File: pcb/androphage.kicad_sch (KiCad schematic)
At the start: 86 parts, among them J1 VIK_OUT, J11 VIK_OUT_SENSOR, J12 Conn_01x04, J13 Conn_01x02, J2 Conn_01x04, J3 USB_C_Receptacle_USB2.0_16P, Q1 AO3401A, Q2 AO3401A, SW00 SW_Push_45deg, SW01 SW_Push_45deg, SW02 SW_Push_45deg, SW03 SW_Push_45deg, SW04 SW_Push_45deg, SW05 SW_Push_45deg, SW10 SW_Push_45deg, SW11 SW_Push_45deg, SW12 SW_Push_45deg, SW13 SW_Push_45deg, SW14 SW_Push_45deg, SW15 SW_Push_45deg, SW20 SW_Push_45deg, SW21 SW_Push_45deg, SW22 SW_Push_45deg, SW23 SW_Push_45deg, SW24 SW_Push_45deg, SW25 SW_Push_45deg, SW30 SW_Push_45deg, SW31 SW_Push_45deg, SW32 SW_Push_45deg, SW33 SW_Push_45deg, SW34 SW_Push_45deg, SW35 SW_Push_45deg, SW6 SW_Push, SW7 SW_SPST, U1 holyiot-18010-no-underside, U2 MCP73832-2-OT, U3 XC6220B331MR, U4 SRV05-4, U6 MCP23017_SS

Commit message: Update key switch footprint.
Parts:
- SW00, SW01, SW02, SW03, SW04, SW10, SW11, SW12, SW13, SW14, SW15, SW20, SW21, SW22, SW23, SW24, SW25, SW31, SW32, SW33, SW34, SW35: footprint key-switches:SW_GLP_Kailh_Choc_V1V2_HotSwap_double -> key-switches:SW_Kailh_Choc_V1V2_HotSwap_PTH_Double
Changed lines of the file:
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@@
 			)
 		)
-		(property "Footprint" "key-switches:SW_GLP_Kailh_Choc_V1V2_HotSwap_double"
+		(property "Footprint" "key-switches:SW_Kailh_Choc_V1V2_HotSwap_PTH_Double"
 			(at 215.9 266.7 0)
 			(effects
@@
 		)
 		(instances
-			(project ""
+			(project "androphage"
 				(path "/99196bd8-ec0c-4029-b5c4-fcab8025953e"
 					(reference "R2")
@@
 		)
 		(instances
-			(project ""
+			(project "androphage"
 				(path "/99196bd8-ec0c-4029-b5c4-fcab8025953e"
 					(reference "R8")
@@
 			)
 		)
-		(property "Footprint" "key-switches:SW_GLP_Kailh_Choc_V1V2_HotSwap_double"
+		(property "Footprint" "key-switches:SW_Kailh_Choc_V1V2_HotSwap_PTH_Double"
 			(at 127 251.46 0)
 			(effects
@@
 		)
 		(instances
-			(project ""
+			(project "androphage"
 				(path "/99196bd8-ec0c-4029-b5c4-fcab8025953e"
 					(reference "U4")
@@
 		)
 		(instances
-			(project ""
+			(project "androphage"
 				(path "/99196bd8-ec0c-4029-b5c4-fcab8025953e"
 					(reference "R9")
@@
 			)
 		)
-		(property "Footprint" "key-switches:SW_GLP_Kailh_Choc_V1V2_HotSwap_double"
+		(property "Footprint" "key-switches:SW_Kailh_Choc_V1V2_HotSwap_PTH_Double"
 			(at 198.12 234.95 0)
 			(effects
@@
 		)
 		(instances
-			(project ""
+			(project "androphage"
 				(path "/99196bd8-ec0c-4029-b5c4-fcab8025953e"
 					(reference "R10")
@@
 			)
 		)
-		(property "Footprint" "key-switches:SW_GLP_Kailh_Choc_V1V2_HotSwap_double"
+		(property "Footprint" "key-switches:SW_Kailh_Choc_V1V2_HotSwap_PTH_Double"
 			(at 215.9 251.46 0)
 			(effects
@@
 			)
 		)
-		(property "Footprint" "key-switches:SW_GLP_Kailh_Choc_V1V2_HotSwap_double"
+		(property "Footprint" "key-switches:SW_Kailh_Choc_V1V2_HotSwap_PTH_Double"
 			(at 215.9 234.95 0)
 			(effects
@@
 		)
 		(instances
-			(project ""
+			(project "androphage"
 				(path "/99196bd8-ec0c-4029-b5c4-fcab8025953e"
 					(reference "D2")
@@
 			)
 		)
-		(property "Footprint" "key-switches:SW_GLP_Kailh_Choc_V1V2_HotSwap_double"
+		(property "Footprint" "key-switches:SW_Kailh_Choc_V1V2_HotSwap_PTH_Double"
 			(at 127 234.95 0)
 			(effects
@@
 		)
 		(instances
-			(project ""
+			(project "androphage"
 				(path "/99196bd8-ec0c-4029-b5c4-fcab8025953e"
 					(reference "SW6")
@@
 			)
 		)
-		(property "Footprint" "key-switches:SW_GLP_Kailh_Choc_V1V2_HotSwap_double"
+		(property "Footprint" "key-switches:SW_Kailh_Choc_V1V2_HotSwap_PTH_Double"
 			(at 144.78 266.7 0)
 			(effects
@@
 		)
 		(instances
-			(project ""
+			(project "androphage"
 				(path "/99196bd8-ec0c-4029-b5c4-fcab8025953e"
 					(reference "R11")
@@
 		)
 		(instances
-			(project ""
+			(project "androphage"
 				(path "/99196bd8-ec0c-4029-b5c4-fcab8025953e"
 					(reference "R12")
@@
 		)
 		(instances
-			(project ""
+			(project "androphage"
 				(path "/99196bd8-ec0c-4029-b5c4-fcab8025953e"
 					(reference "U2")
@@
 		)
 		(instances
-			(project ""
+			(project "androphage"
 				(path "/99196bd8-ec0c-4029-b5c4-fcab8025953e"
 					(reference "J2")
@@
 			)
 		)
-		(property "Footprint" "key-switches:SW_GLP_Kailh_Choc_V1V2_HotSwap_double"
+		(property "Footprint" "key-switches:SW_Kailh_Choc_V1V2_HotSwap_PTH_Double"
 			(at 162.56 234.95 0)
 			(effects
@@
 			)
 		)
-		(property "Footprint" "key-switches:SW_GLP_Kailh_Choc_V1V2_HotSwap_double"
+		(property "Footprint" "key-switches:SW_Kailh_Choc_V1V2_HotSwap_PTH_Double"
 			(at 127 219.71 0)
 			(effects
@@
 			)
 		)
-		(property "Footprint" "key-switches:SW_GLP_Kailh_Choc_V1V2_HotSwap_double"
+		(property "Footprint" "key-switches:SW_Kailh_Choc_V1V2_HotSwap_PTH_Double"
 			(at 180.34 266.7 0)
 			(effects
@@
 			)
 		)
-		(property "Footprint" "key-switches:SW_GLP_Kailh_Choc_V1V2_HotSwap_double"
+		(property "Footprint" "key-switches:SW_Kailh_Choc_V1V2_HotSwap_PTH_Double"
 			(at 144.78 251.46 0)
 			(effects
@@
 		)
 		(instances
-			(project ""
+			(project "androphage"
 				(path "/99196bd8-ec0c-4029-b5c4-fcab8025953e"
 					(reference "JP1")
@@
 			)
 		)
-		(property "Footprint" "key-switches:SW_GLP_Kailh_Choc_V1V2_HotSwap_double"
+		(property "Footprint" "key-switches:SW_Kailh_Choc_V1V2_HotSwap_PTH_Double"
 			(at 198.12 219.71 0)
 			(effects
@@
 			)
 		)
-		(property "Footprint" "key-switches:SW_GLP_Kailh_Choc_V1V2_HotSwap_double"
+		(property "Footprint" "key-switches:SW_Kailh_Choc_V1V2_HotSwap_PTH_Double"
 			(at 144.78 234.95 0)
 			(effects
@@
 			)
 		)
-		(property "Footprint" "key-switches:SW_GLP_Kailh_Choc_V1V2_HotSwap_double"
+		(property "Footprint" "key-switches:SW_Kailh_Choc_V1V2_HotSwap_PTH_Double"
 			(at 180.34 234.95 0)
 			(effects
@@
 		)
 		(instances
-			(project ""
+			(project "androphage"
 				(path "/99196bd8-ec0c-4029-b5c4-fcab8025953e"
 					(reference "J3")
@@
 			)
 		)
-		(property "Footprint" "key-switches:SW_GLP_Kailh_Choc_V1V2_HotSwap_double"
+		(property "Footprint" "key-switches:SW_Kailh_Choc_V1V2_HotSwap_PTH_Double"
 			(at 180.34 251.46 0)
 			(effects
@@
 			)
 		)
-		(property "Footprint" "key-switches:SW_GLP_Kailh_Choc_V1V2_HotSwap_double"
+		(property "Footprint" "key-switches:SW_Kailh_Choc_V1V2_HotSwap_PTH_Double"
 			(at 162.56 266.7 0)
 			(effects
@@
 			)
 		)
-		(property "Footprint" "key-switches:SW_GLP_Kailh_Choc_V1V2_HotSwap_double"
+		(property "Footprint" "key-switches:SW_Kailh_Choc_V1V2_HotSwap_PTH_Double"
 			(at 198.12 266.7 0)
 			(effects
@@
 		)
 		(instances
-			(project ""
+			(project "androphage"
 				(path "/99196bd8-ec0c-4029-b5c4-fcab8025953e"
 					(reference "Q1")
@@
 			)
 		)
-		(property "Footprint" "key-switches:SW_GLP_Kailh_Choc_V1V2_HotSwap_double"
+		(property "Footprint" "key-switches:SW_Kailh_Choc_V1V2_HotSwap_PTH_Double"
 			(at 162.56 251.46 0)
 			(effects
@@
 			)
 		)
-		(property "Footprint" "key-switches:SW_GLP_Kailh_Choc_V1V2_HotSwap_double"
+		(property "Footprint" "key-switches:SW_Kailh_Choc_V1V2_HotSwap_PTH_Double"
 			(at 144.78 219.71 0)
 			(effects
@@
 		)
 		(instances
-			(project ""
+			(project "androphage"
 				(path "/99196bd8-ec0c-4029-b5c4-fcab8025953e"
 					(reference "U3")
@@
 			)
 		)
-		(property "Footprint" "key-switches:SW_GLP_Kailh_Choc_V1V2_HotSwap_double"
+		(property "Footprint" "key-switches:SW_Kailh_Choc_V1V2_HotSwap_PTH_Double"
 			(at 162.56 219.71 0)
 			(effects
@@
 		)
 		(instances
-			(project ""
+			(project "androphage"
 				(path "/99196bd8-ec0c-4029-b5c4-fcab8025953e"
 					(reference "SW7")
@@
 			)
 		)
-		(property "Footprint" "key-switches:SW_GLP_Kailh_Choc_V1V2_HotSwap_double"
+		(property "Footprint" "key-switches:SW_Kailh_Choc_V1V2_HotSwap_PTH_Double"
 			(at 198.12 251.46 0)
 			(effects
@@
 		)
 		(instances
-			(project ""
+			(project "androphage"
 				(path "/99196bd8-ec0c-4029-b5c4-fcab8025953e"
 					(reference "D1")
@@
 			)
 		)
-		(property "Footprint" "key-switches:SW_GLP_Kailh_Choc_V1V2_HotSwap_double"
+		(property "Footprint" "key-switches:SW_Kailh_Choc_V1V2_HotSwap_PTH_Double"
 			(at 180.34 219.71 0)
 			(effects

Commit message: Restart PCB design.
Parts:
- removed D12, D13, D14, D15, D16, D17, D18, D19, D2, D20, D21, D22, D23, D24, D25, D26, D27, D28, D29, D3, D4, D5, D6, D7: 1N4148W, Diode_SMD:D_SOD-123, symbol Diode:1N4148W
- FB_USB_01: renamed from FB2; value ~ -> (none)
- U_MAT_01: renamed from U6; symbol Interface_Expansion:MCP23017_SS -> Interface_Expansion:MCP23017x-x-SS
- renumbered D8 to D_LED_01, D9 to D_LED_02, D10 to D_LED_03, D11 to D_LED_04, D1 to D_POW_1, F2 to F_USB_02, JP1 to JP_CHG_01, J13 to J_BAT_01, J2 to J_OLED_01, J12 to J_SWD_01, J3 to J_USB_01, J1 to J_VIK_01, J11 to J_VIK_02, Q2 to Q_EXT_01, Q1 to Q_POW_1, R11 to R_CHG_01, R12 to R_CHG_02, R17 to R_EXT_01, R7 to R_MAT_01, R6 to R_MAT_02, R5 to R_MAT_11, R4 to R_MAT_12, R2 to R_MAT_21, R3 to R_MAT_22, R1 to R_MAT_31, R15 to R_MON_01, R16 to R_MON_02, R10 to R_POW_01, R8 to R_USB_01, R9 to R_USB_02, SW7 to SW_BAT_01, SW6 to SW_RST1, SW00 to S_MAT_00, SW01 to S_MAT_01, SW02 to S_MAT_02, SW03 to S_MAT_03, SW04 to S_MAT_04, SW05 to S_MAT_05, SW10 to S_MAT_10, SW11 to S_MAT_11, SW12 to S_MAT_12, SW13 to S_MAT_13, SW14 to S_MAT_14, SW15 to S_MAT_15, SW20 to S_MAT_20, SW21 to S_MAT_21, SW22 to S_MAT_22, SW23 to S_MAT_23, SW24 to S_MAT_24, SW25 to S_MAT_25, SW30 to S_MAT_30, SW31 to S_MAT_31, SW32 to S_MAT_32, SW33 to S_MAT_33, SW34 to S_MAT_34, SW35 to S_MAT_35, U2 to U_CHG_01, U1 to U_MCU_1, U3 to U_POW_01, U4 to U_USB_01
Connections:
- net C0: now also U_MAT_01.1 (GPB0); no longer U_MAT_01.21 (GPA0)
- net C1: now also U_MAT_01.2 (GPB1); no longer U_MAT_01.22 (GPA1)
- net C2: now also U_MAT_01.3 (GPB2); no longer U_MAT_01.23 (GPA2)
- net C3: now also U_MAT_01.4 (GPB3); no longer U_MAT_01.24 (GPA3)
- net C4: now also U_MAT_01.5 (GPB4); no longer U_MAT_01.25 (GPA4)
- net C5: now also U_MAT_01.6 (GPB5); no longer U_MAT_01.26 (GPA5)
- net GND: no longer R_MAT_01.1, R_MAT_02.2, U_MAT_01.17 (A2)
- net GNDPWR: now also J_USB_01.SH (SHIELD); no longer J_USB_01.S1 (SHIELD)
- net R0: now also S_MAT_00.2, S_MAT_01.2, S_MAT_02.2, S_MAT_03.2, S_MAT_04.2, S_MAT_05.2, U_MAT_01.21 (GPA0); no longer U_MAT_01.1 (GPB0)
- net R1: now also S_MAT_10.2, S_MAT_11.2, S_MAT_12.2, S_MAT_13.2, S_MAT_14.2, S_MAT_15.2, U_MAT_01.22 (GPA1); no longer U_MAT_01.2 (GPB1)
- net R2: now also S_MAT_20.2, S_MAT_21.2, S_MAT_22.2, S_MAT_23.2, S_MAT_24.2, S_MAT_25.2, U_MAT_01.23 (GPA2); no longer U_MAT_01.3 (GPB2)
- net R3: now also S_MAT_30.2, S_MAT_31.2, S_MAT_32.2, S_MAT_33.2, S_MAT_34.2, S_MAT_35.2, U_MAT_01.24 (GPA3); no longer U_MAT_01.4 (GPB3)
- net SCL: now also U_MAT_01.13 (SDA); no longer U_MAT_01.12 (SCK)
- net SDA: now also U_MAT_01.12 (SCK); no longer U_MAT_01.13 (SDA)
- net at R_MAT_21.1, R_MAT_22.2: now also U_MAT_01.17 (A2); no longer U_MAT_01.15 (A0)
- new net: R_MAT_01.1, R_MAT_02.2, U_MAT_01.15 (A0)
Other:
- moved on the sheet: JP_CHG_01, R_CHG_01, R_MAT_01, R_MAT_02, R_MAT_11, R_MAT_12, R_MAT_21, R_MAT_22, R_MAT_31, R_USB_01, R_USB_02

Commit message: Work on PCBs.
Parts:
- removed J_OLED_01: Conn_01x04, Connector_JST:JST_GH_SM04B-GHS-TB_1x04-1MP_P1.25mm_Horizontal, symbol Connector_Generic:Conn_01x04
- added J_VIK_03: VIK_OUT_DISP, vik:vik-keyboard-connector-horizontal, symbol vik:vik-keyboard-connector
- D_LED_01, D_LED_02, D_LED_03, D_LED_04: now not fitted; now left out of the parts list
- J_VIK_01: value VIK_OUT -> VIK_OUT_INTC
- J_VIK_02: value VIK_OUT_SENSOR -> VIK_OUT_SENS
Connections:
- net CS_PMW2: now also U_MCU_1.35 ([L]_P1.06); no longer U_MCU_1.39 ([L]_P1.02)
- net GND: now also J_SWD_01.3 (Pin_3), J_VIK_03.2 (GND); no longer J_SWD_01.2 (Pin_2)
- net GP12: now also U_MCU_1.51 (P0.23); no longer U_MCU_1.36 ([L]_P1.04)
- net GP22: now also U_MCU_1.50 (P0.21); no longer U_MCU_1.41 ([L]_P1.03)
- net INT_PMW1: now also U_MCU_1.39 ([L]_P1.02); no longer U_MCU_1.35 ([L]_P1.06)
- net MISO: now also J_VIK_03.11 (MISO)
- net MOSI: now also J_VIK_03.8 (MOSI)
- net SCL: now also J_VIK_03.4 (SCL)
- net SCLK: now also J_VIK_03.12 (SCLK)
- net SDA: now also J_VIK_03.3 (SDA)
- net SWC: now also J_SWD_01.2 (Pin_2); no longer J_SWD_01.4 (Pin_4)
- net SWD: now also J_SWD_01.4 (Pin_4); no longer J_SWD_01.3 (Pin_3)
- net VDD: now also J_VIK_03.1 (3V3)
- net VEXT: now also J_VIK_03.6 (5V)
- net at U_MCU_1.48 (Reset/P0.18): now also SW_RST1.1
- net GP32: now reaches U_MCU_1.49 (P0.19)
- net GP32: now also J_VIK_03.9 (GP_AD2); no longer SW_RST1.1
- net RGB_DO3: now reaches U_MCU_1.6 ([L]_A1_P0.03)
- net RGB_DO3: now also J_VIK_03.5 (RGB_DO)
- new net CS_DIS1: J_VIK_03.10 (SPI_CS), U_MCU_1.36 ([L]_P1.04)
- new net GP31: J_VIK_03.7 (GP_AD1), U_MCU_1.41 ([L]_P1.03)
- no-connect marks 24 -> 20
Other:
- note added: "VIK Display"
- note removed: "OLED"
- moved on the sheet: J_BAT_01, J_SWD_01, J_VIK_01, J_VIK_02, SW_BAT_01, SW_RST1

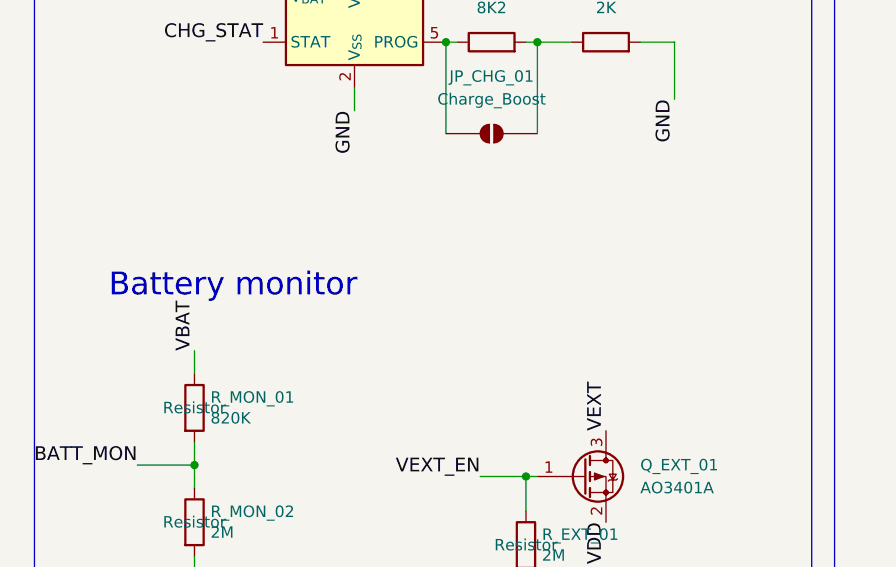
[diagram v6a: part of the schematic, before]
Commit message: Refine USB port placement.
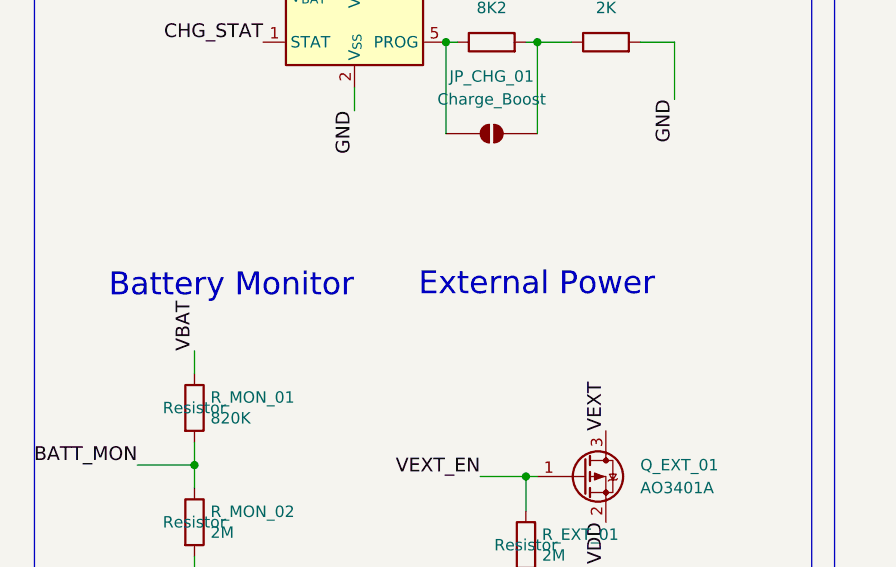
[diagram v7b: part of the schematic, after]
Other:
- note added: "Battery Monitor"
- note added: "External Power"
- note removed: "Battery monitor"
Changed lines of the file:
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@@
 		)
 	)
-	(text "Battery monitor"
+	(text "Battery Monitor"
 		(exclude_from_sim no)
 		(at 22.225 240.665 0)
@@
 		(effects
 			(font
+				(size 2.54 2.54)
+			)
+			(justify left bottom)
+		)
+	)
+	(text "External Power"
+		(exclude_from_sim no)
+		(at 56.642 240.538 0)
+		(effects
+			(font

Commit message: Work on PCBs.
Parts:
- removed D_LED_01, D_LED_02, D_LED_03, D_LED_04: SK6812MINI, LED_SMD:LED_SK6812MINI_PLCC4_3.5x3.5mm_P1.75mm, symbol LED:SK6812MINI
- removed D_POW_1: 1N5819WS, Diode_SMD:D_SOD-323, symbol Diode:1N5819WS
- removed FB_USB_01: (no value), Inductor_SMD:L_0805_2012Metric, symbol Device:FerriteBead
- removed F_USB_02: SMD0805-050-16V, Fuse:Fuse_0805_2012Metric, symbol Device:Fuse
- removed JP_CHG_01: Charge_Boost, Jumper:SolderJumper-2_P1.3mm_Open_RoundedPad1.0x1.5mm, symbol Jumper:SolderJumper_2_Open
- removed J_BAT_01: Conn_01x02, Connector_JST:JST_GH_SM02B-GHS-TB_1x02-1MP_P1.25mm_Horizontal, symbol Connector_Generic:Conn_01x02
- removed J_SWD_01: Conn_01x04, Connector_PinSocket_2.54mm:PinSocket_1x04_P2.54mm_Vertical, symbol Connector_Generic:Conn_01x04
- removed J_USB_01: USB_C_Receptacle_USB2.0_16P, Connector_USB:USB_C_Receptacle_HRO_TYPE-C-31-M-12, symbol Connector:USB_C_Receptacle_USB2.0_16P
- removed J_VIK_01: VIK_OUT_INTC, vik:vik-keyboard-connector-horizontal, symbol vik:vik-keyboard-connector
- removed J_VIK_02: VIK_OUT_SENS, vik:vik-keyboard-connector-horizontal, symbol vik:vik-keyboard-connector
- removed J_VIK_03: VIK_OUT_DISP, vik:vik-keyboard-connector-horizontal, symbol vik:vik-keyboard-connector
- removed Q_EXT_01, Q_POW_1: AO3401A, Package_TO_SOT_SMD:SOT-23, symbol Transistor_FET:AO3401A
- removed R_CHG_01: 8K2, Resistor_SMD:R_0201_0603Metric_Pad0.64x0.40mm_HandSolder, symbol Device:R
- removed R_CHG_02: 2K, Resistor_SMD:R_0201_0603Metric_Pad0.64x0.40mm_HandSolder, symbol Device:R
- removed R_EXT_01, R_MON_02: 2M, Resistor_SMD:R_0603_1608Metric, symbol Device:R
- removed R_MAT_01, R_MAT_02, R_MAT_11, R_MAT_12, R_MAT_21, R_MAT_22, R_MAT_31: 10K, Resistor_SMD:R_0201_0603Metric_Pad0.64x0.40mm_HandSolder, symbol Device:R
- removed R_MON_01: 820K, Resistor_SMD:R_0603_1608Metric, symbol Device:R
- removed R_POW_01: 100K, Resistor_SMD:R_0201_0603Metric_Pad0.64x0.40mm_HandSolder, symbol Device:R
- removed R_USB_01, R_USB_02: 5.1K, Resistor_SMD:R_0201_0603Metric_Pad0.64x0.40mm_HandSolder, symbol Device:R
- removed SW_BAT_01: SW_SPST, library:AS11CH, symbol Switch:SW_SPST
- removed SW_RST1: SW_Push, Button_Switch_SMD:SW_Push_1P1T_NO_E-Switch_TL3301NxxxxxG, symbol Switch:SW_Push
- removed S_MAT_00, S_MAT_01, S_MAT_02, S_MAT_03, S_MAT_04, S_MAT_10, S_MAT_11, S_MAT_12, S_MAT_13, S_MAT_14, S_MAT_15, S_MAT_20, S_MAT_21, S_MAT_22, S_MAT_23, S_MAT_24, S_MAT_25, S_MAT_31, S_MAT_32, S_MAT_33, S_MAT_34, S_MAT_35: SW_Push_45deg, key-switches:SW_Kailh_Choc_V1V2_HotSwap_PTH_Double, symbol Switch:SW_Push_45deg
- removed S_MAT_05, S_MAT_30: SW_Push_45deg, symbol Switch:SW_Push_45deg
- removed U_CHG_01: MCP73832-2-OT, Package_TO_SOT_SMD:SOT-23-5, symbol Battery_Management:MCP73832-2-OT
- removed U_MAT_01: MCP23017_SS, Package_SO:SSOP-28_5.3x10.2mm_P0.65mm, symbol Interface_Expansion:MCP23017x-x-SS
- removed U_MCU_1: holyiot-18010-no-underside, mcu:holyiot-18010-no-underside, symbol mcu:holyiot-18010-no-underside
- removed U_POW_01: XC6220B331MR, Package_TO_SOT_SMD:SOT-23-5, symbol Regulator_Linear:XC6220B331MR
- removed U_USB_01: SRV05-4, Package_TO_SOT_SMD:SOT-23-6, symbol Power_Protection:SRV05-4
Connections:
- no-connect marks 20 -> 0
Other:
- added sheet Control_Board (control_board.kicad_sch)
- added sheet Power_Board (power_board.kicad_sch)
- added sheet Switch_Board (switch_board.kicad_sch)
- note added: "Control Board"
- note added: "Power Board"
- note added: "Switch Board"
- note removed: "Battery"
- note removed: "Battery Monitor"
- note removed: "External Power"
- note removed: "LEDs"
- note removed: "LiPo Charging"
- note removed: "Port"
- note removed: "Power and Filtering"
- note removed: "RProg = 1000/iBat iBat in amps RProg iBAT 10k 100mA 5k 200mA 2.5k 400mA 2k 500mA 1.25k 800mA"
- note removed: "SWD"
- note removed: "USB ESD"
- note removed: "VBUS ESD"
- note removed: "VIK Display"
- note removed: "VIK Interconnect"
- note removed: "VIK Trackball Sensor"
